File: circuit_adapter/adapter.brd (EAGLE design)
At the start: 24 x 36.5 mm, 17 parts, among them CN3 MICROSD_BARE, CN4 VIRTUALGIMAL, CN5 MICROSD_WM11190CT-ND, X1 2510-

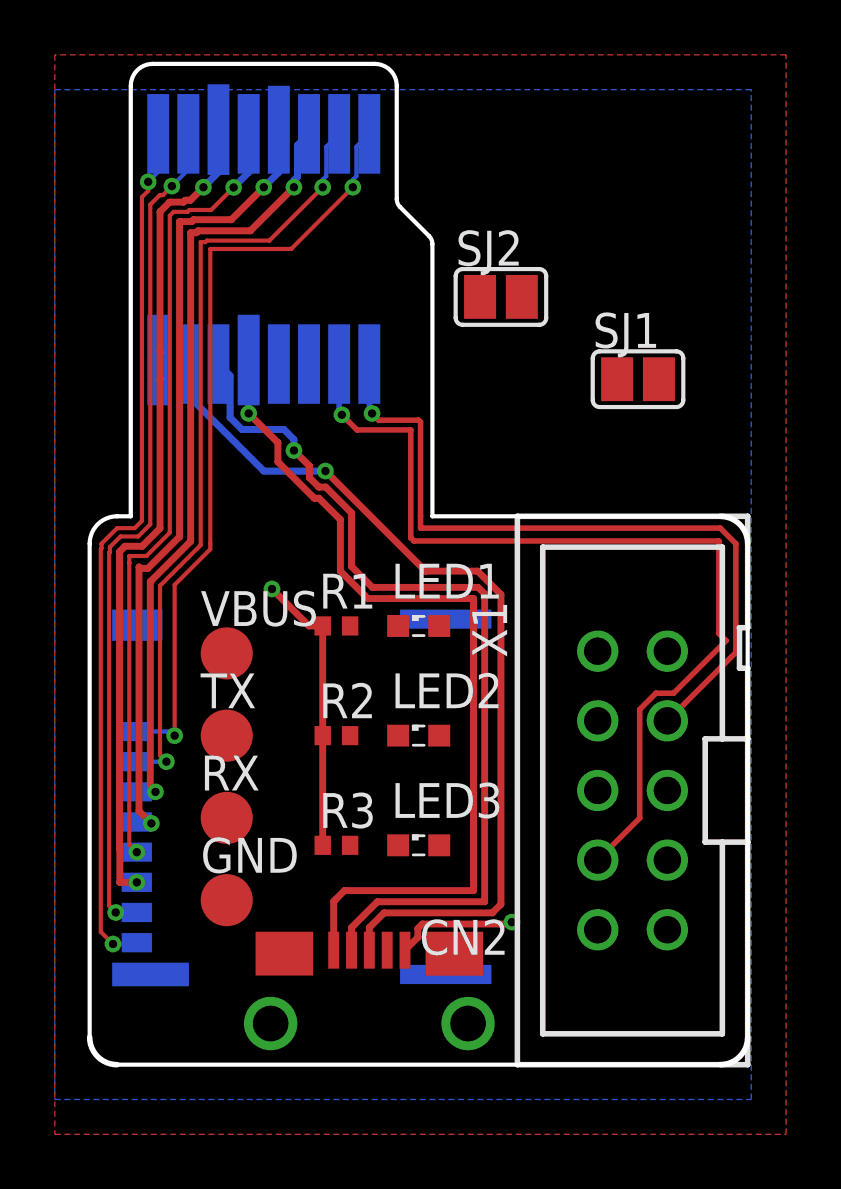
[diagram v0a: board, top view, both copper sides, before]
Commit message: Modified circuit adapter
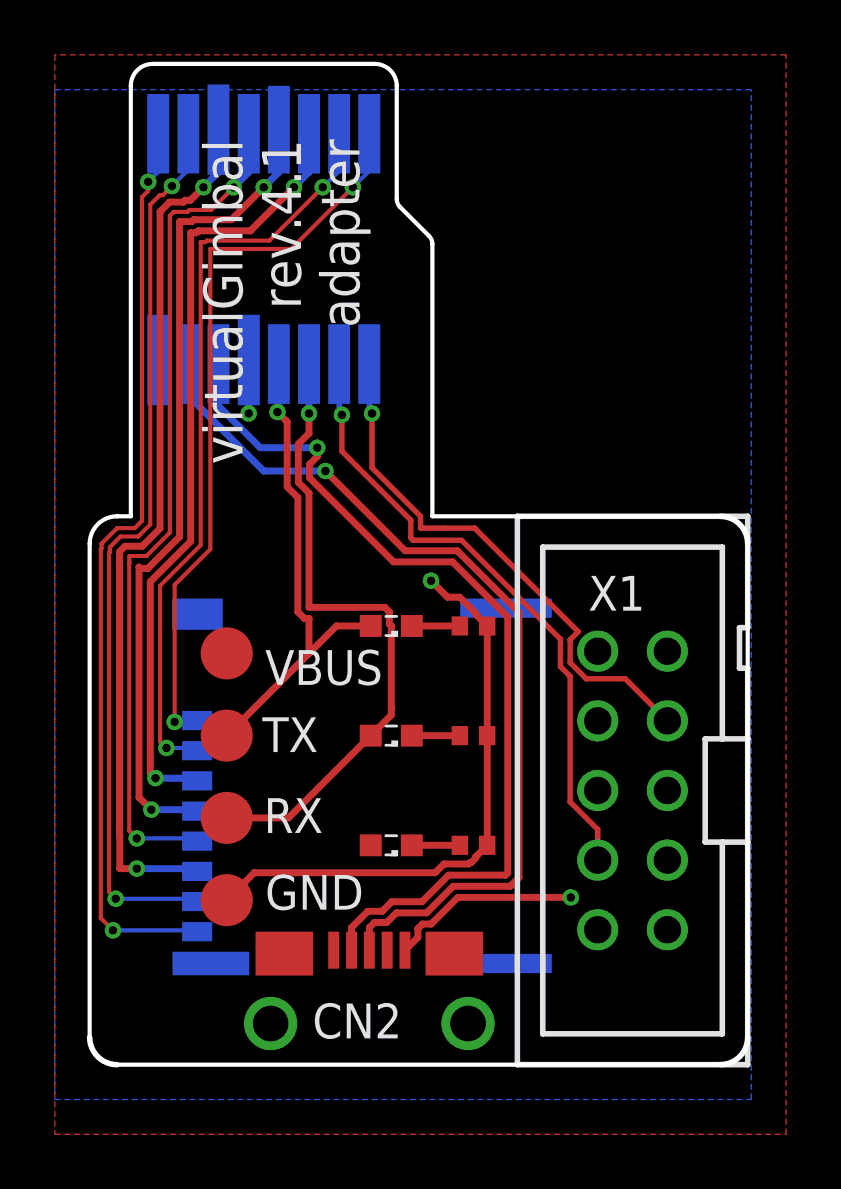
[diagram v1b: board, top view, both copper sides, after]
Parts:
- removed SJ1, SJ2: (no value), jumper:SJ
- moved R1 9.43 mm to (14.0, 8.00), turned to 180 degrees
- moved LED1 8.06 mm to (11.0, 8.00), turned to 180 degrees
- moved R2 6.40 mm to (14.0, 16.0), turned to 180 degrees
- moved R3 6.40 mm to (14.0, 12.0), turned to 180 degrees
- moved LED2 4.12 mm to (11.0, 16.0), turned to 180 degrees
- moved LED3 4.12 mm to (11.0, 12.0), turned to 180 degrees
- moved CN5 2.24 mm to (16.9, 17.0)
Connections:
- removed net N$12: LED2.A, SJ1.1
- removed net N$13: LED3.A, SJ2.1
- net RX1: now also LED3.A; no longer SJ2.2
- net TX1: now also LED2.A; no longer SJ1.2
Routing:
- net VBUS: track 32.2 -> 1.95 mm
- net RX1: track 0.00 -> 23.5 mm, vias 0 -> 1
- net TX1: track 0.00 -> 18.1 mm, vias 0 -> 1
- net DGND: track 14.9 -> 28.1 mm
- net C2D: track 33.9 -> 23.0 mm
- net C2CK: track 26.8 -> 19.7 mm
- net N$3: track 0.00 -> 1.75 mm
- net N$2: track 0.00 -> 1.75 mm
- net N$1: track 0.00 -> 1.75 mm
- net N$9: track 30.3 -> 32.1 mm
- net N$8: track 29.2 -> 31.0 mm
- net N$10: track 30.9 -> 32.6 mm
- net N$11: track 31.9 -> 33.6 mm
- net N$4: track 28.1 -> 27.0 mm
- net N$7: track 29.5 -> 30.1 mm
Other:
- board text added: "virtualGimbal rev.4.1 adapter"
